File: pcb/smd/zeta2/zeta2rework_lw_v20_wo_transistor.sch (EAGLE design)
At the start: 95 parts, among them IC1 MAX6520, U5 DS18B20U+

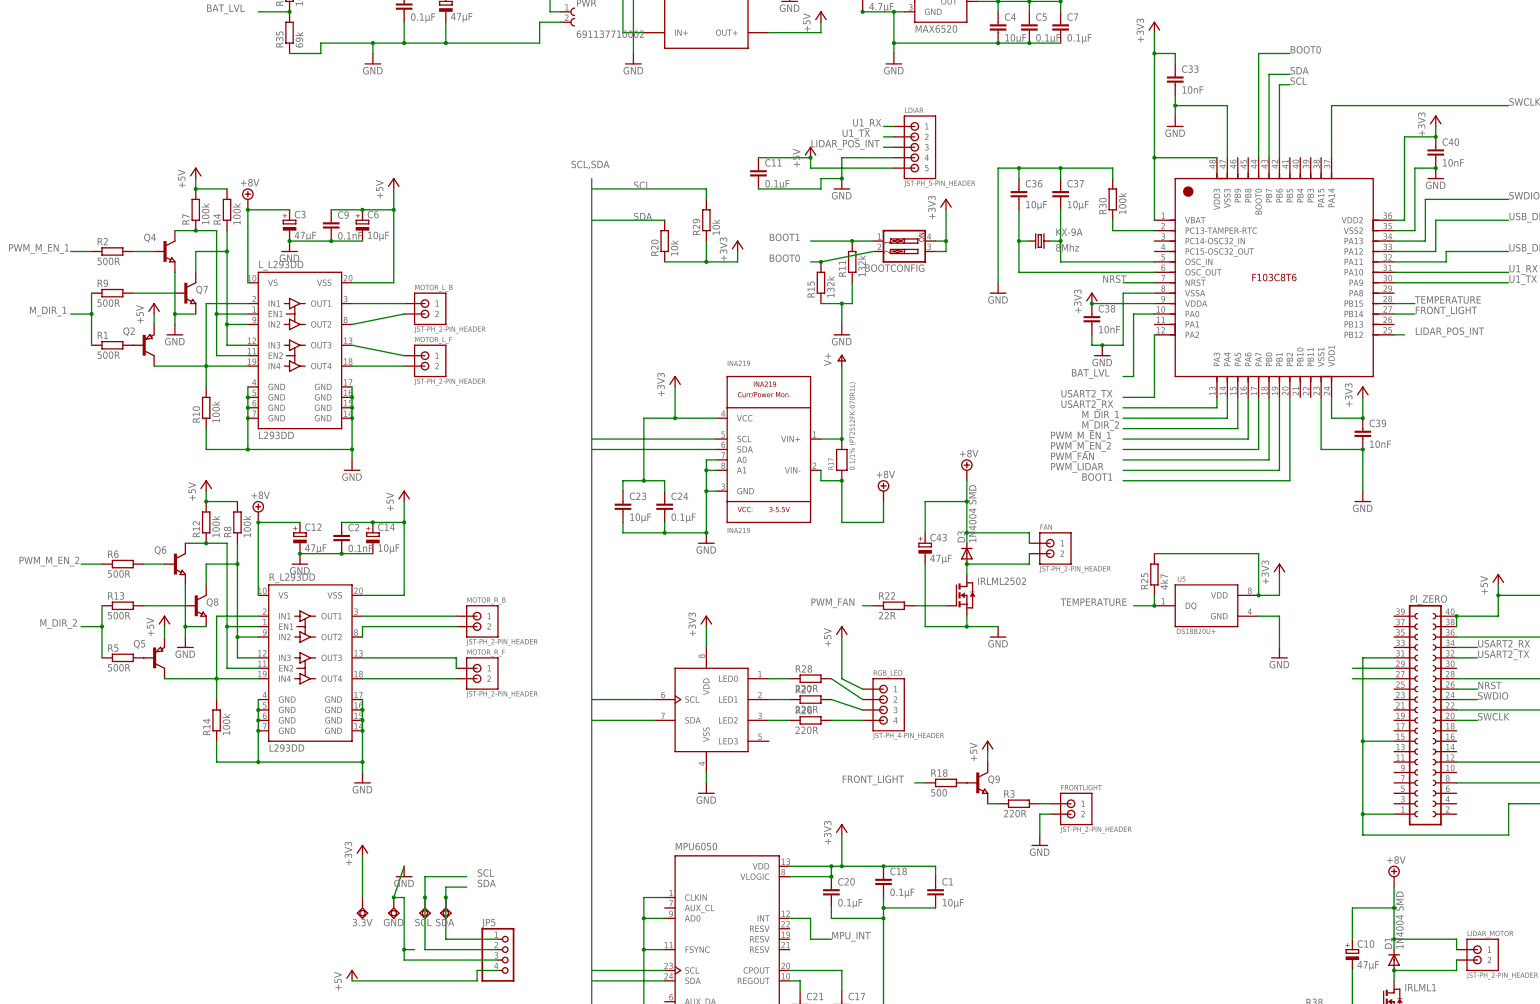
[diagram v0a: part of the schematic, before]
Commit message: removed l293d transistors
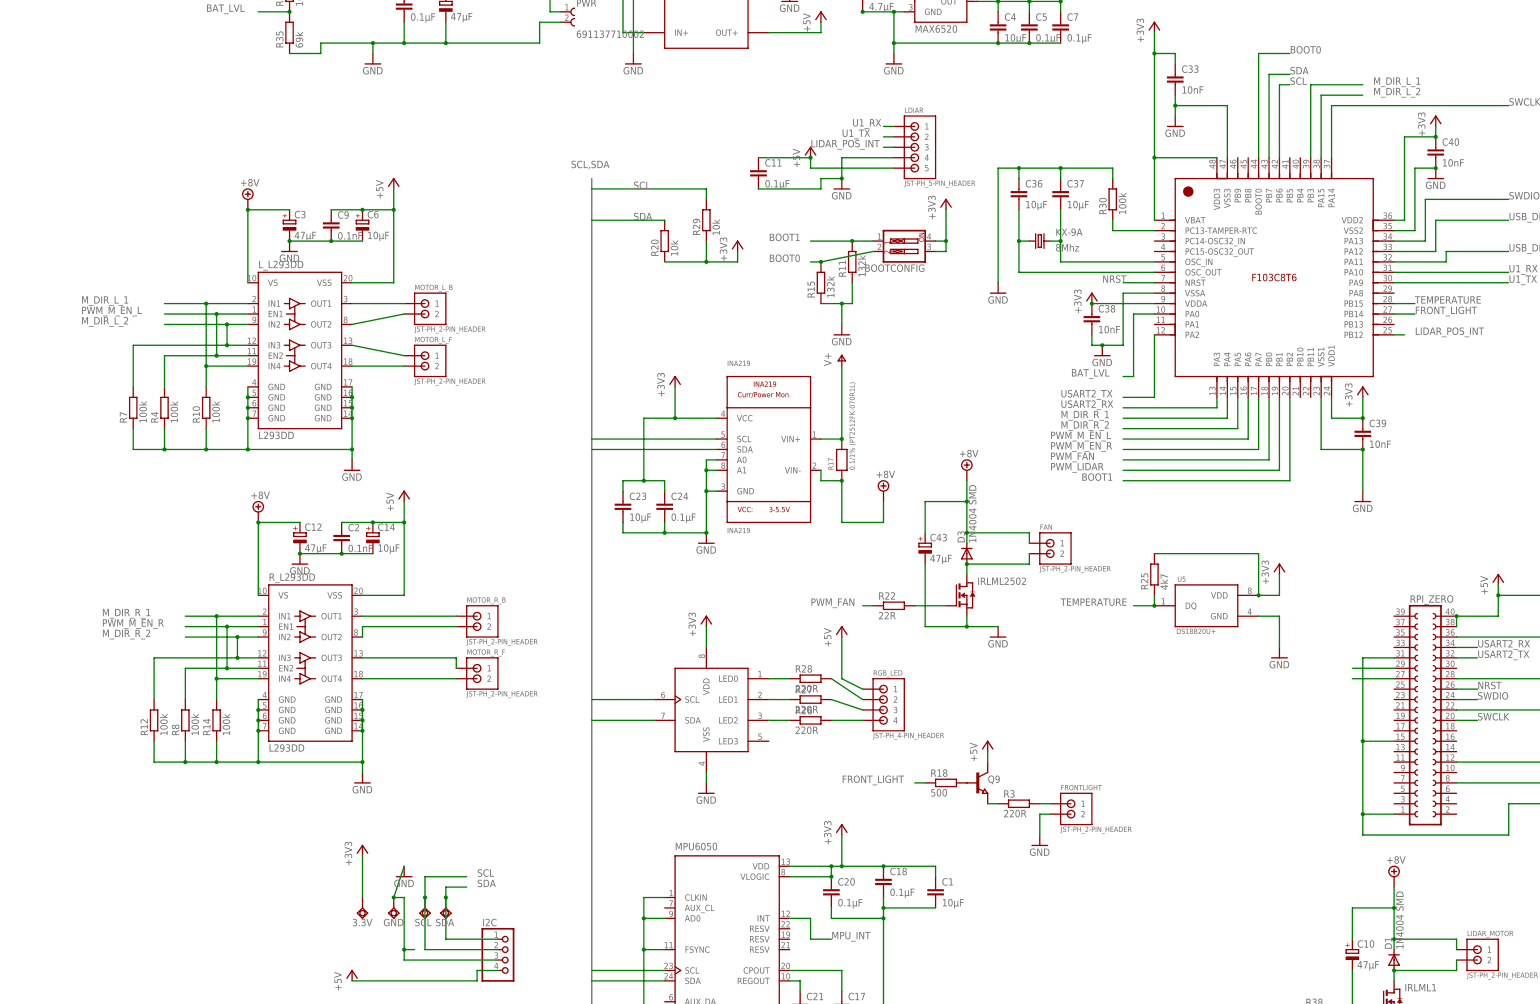
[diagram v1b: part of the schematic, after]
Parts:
- removed Q2, Q5: (no value), semicon-smd-ipc:PNP-TRANSISTOR_SOT23
- removed Q4, Q6, Q7, Q8: (no value), semicon-smd-ipc:NPN-TRANSISTOR_SOT23
- removed R1, R13, R2, R5, R6, R9: 500R, rcl:R-EU_R0603
- renumbered JP5 to I2C, PI_ZERO to RPI_ZERO
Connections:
- removed net M_DIR_1: R1.1, R9.1, STM32F103CB.PA4
- removed net M_DIR_2: R13.1, R5.1, STM32F103CB.PA5
- removed net N$1: L_L293DD.IN2, L_L293DD.IN3, Q7.C, R4.1
- removed net N$10: Q2.B, R1.2
- removed net N$11: Q4.B, R2.2
- removed net N$12: Q7.B, R9.2
- removed net N$13: Q5.B, R5.2
- removed net N$14: Q6.B, R6.2
- removed net N$15: Q8.B, R13.2
- removed net N$5: L_L293DD.IN1, L_L293DD.IN4, Q2.C, R10.2
- removed net N$6: Q8.C, R8.1, R_L293DD.IN2, R_L293DD.IN3
- removed net N$7: Q5.C, R14.2, R_L293DD.IN1, R_L293DD.IN4
- removed net N$8: L_L293DD.EN1, L_L293DD.EN2, Q4.C, R7.1
- removed net N$9: Q6.C, R12.1, R_L293DD.EN1, R_L293DD.EN2
- removed net PWM_M_EN_1: R2.1, STM32F103CB.PA6
- removed net PWM_M_EN_2: R6.1, STM32F103CB.PA7
- new net M_DIR_L_1: L_L293DD.IN1, L_L293DD.IN4, R10.2, STM32F103CB.PB3
- new net M_DIR_L_2: L_L293DD.IN2, L_L293DD.IN3, R7.2, STM32F103CB.PA15
- new net M_DIR_R_1: R14.2, R_L293DD.IN1, R_L293DD.IN4, STM32F103CB.PA4
- new net M_DIR_R_2: R12.2, R_L293DD.IN2, R_L293DD.IN3, STM32F103CB.PA5
- new net PWM_M_EN_L: L_L293DD.EN1, L_L293DD.EN2, R4.2, STM32F103CB.PA6
- new net PWM_M_EN_R: R8.2, R_L293DD.EN1, R_L293DD.EN2, STM32F103CB.PA7
- net +5V: no longer Q2.E, Q5.E, R12.2, R4.2, R7.2, R8.2
- net GND: now also R12.1, R4.1, R7.1, R8.1; no longer Q4.E, Q6.E, Q7.E, Q8.E
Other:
- moved on the sheet: R12, R4, R7, R8
